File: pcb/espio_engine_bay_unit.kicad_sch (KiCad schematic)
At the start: 43 parts, among them U1 MCP2562-E-SN, U5 LF50CPT-TR

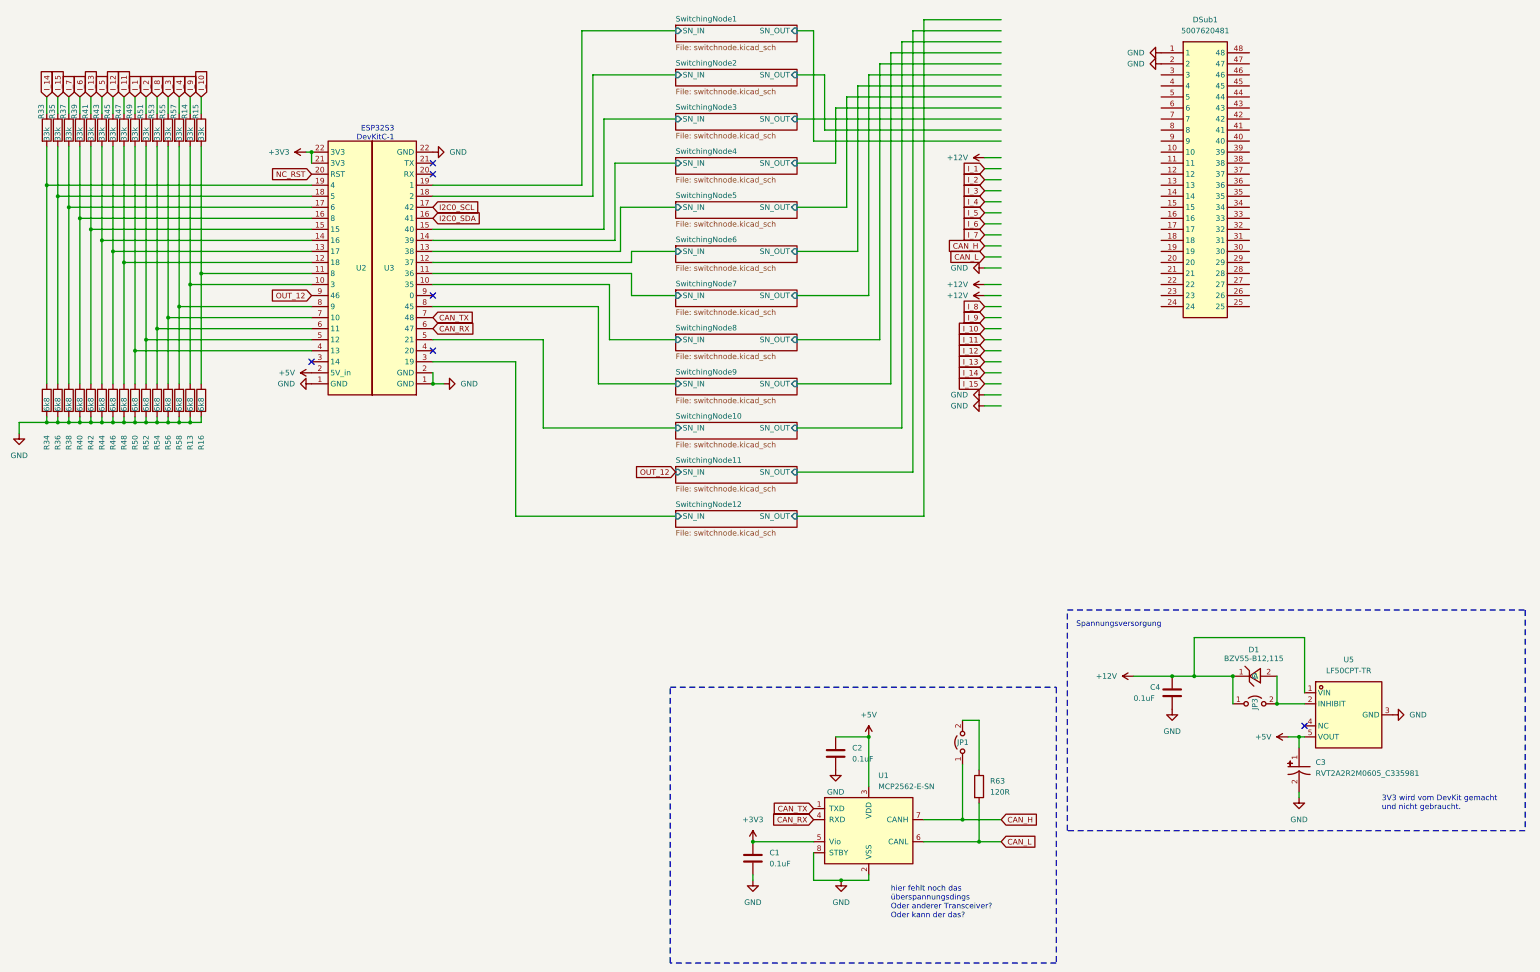
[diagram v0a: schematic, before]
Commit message: Add counters to ebu, update schematic
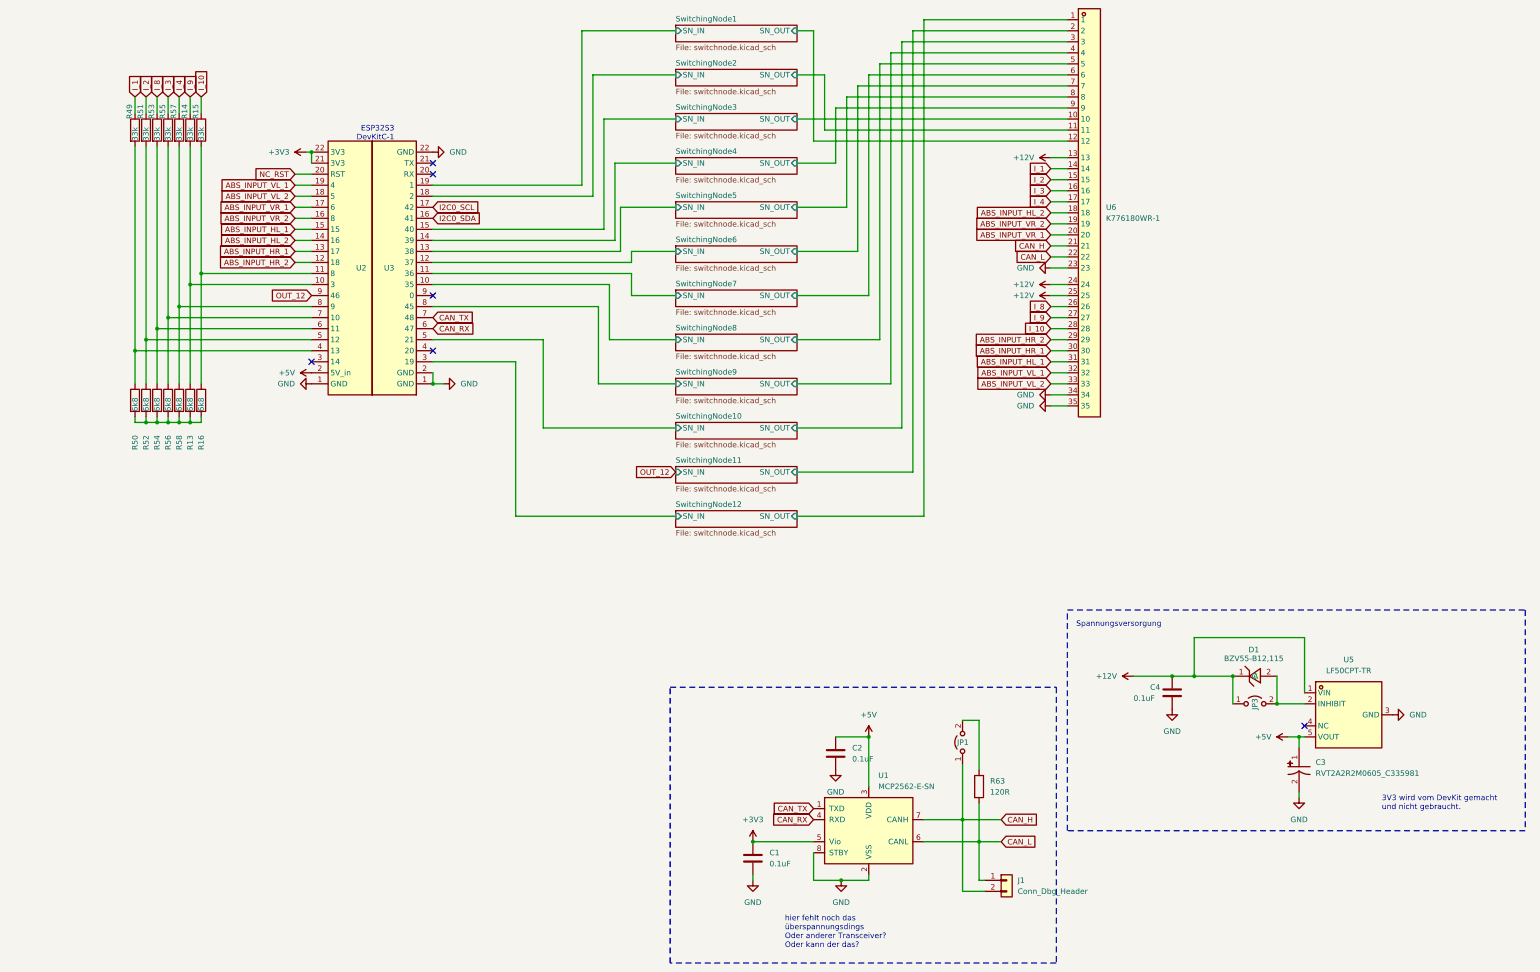
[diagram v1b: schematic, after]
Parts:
- removed DSub1: 5007620481, lcsc:CONN-TH_5007620481, symbol lcsc:5007620481
- removed R33, R35, R37, R39, R41, R43, R45, R47: 33k, Resistor_SMD:R_0603_1608Metric, symbol Device:R
- removed R34, R36, R38, R40, R42, R44, R46, R48: 6k8, Resistor_SMD:R_0603_1608Metric, symbol Device:R
- added J1: Conn_Dbg_Header, Connector_PinHeader_2.54mm:PinHeader_1x02_P2.54mm_Vertical_SMD_Pin1Left, symbol Connector_Generic:Conn_01x02
- added U6: K776180WR-1, lcsc:CONN-TH_35P-P4.00_K776180WR-2, symbol lcsc:K776180WR-1
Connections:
- net +12V: now also U6.13, U6.24, U6.25
- net CAN_H: now also J1.2 (Pin_2), U6.21
- net CAN_L: now also J1.1 (Pin_1), U6.22
- net GND: now also U6.23, U6.34, U6.35; no longer R13.2, R16.2, R50.2, R52.2, R54.2, R56.2, R58.2
- net I_1: now also U6.14
- net I_10: now also U6.28
- net I_2: now also U6.15
- net I_3: now also U6.16
- net I_4: now also U6.17
- net I_8: now also U6.26
- net I_9: now also U6.27
- net SwitchingNode1/SN_OUT: now also U6.12
- net SwitchingNode10/SN_OUT: now also U6.3
- net SwitchingNode11/SN_OUT: now also U6.2
- net SwitchingNode12/SN_OUT: now also U6.1
- net SwitchingNode2/SN_OUT: now also U6.11
- net SwitchingNode3/SN_OUT: now also U6.10
- net SwitchingNode4/SN_OUT: now also U6.9
- net SwitchingNode5/SN_OUT: now also U6.8
- net SwitchingNode6/SN_OUT: now also U6.7
- net SwitchingNode7/SN_OUT: now also U6.6
- net SwitchingNode8/SN_OUT: now also U6.5
- net SwitchingNode9/SN_OUT: now also U6.4
- net ABS_INPUT_HR_2: now reaches U2.12 (18)
- net ABS_INPUT_HR_2: now also U6.29
- net ABS_INPUT_HR_1: now reaches U2.13 (17)
- net ABS_INPUT_HR_1: now also U6.30
- net ABS_INPUT_HL_2: now reaches U2.14 (16)
- net ABS_INPUT_HL_2: now also U6.18
- net ABS_INPUT_HL_1: now reaches U2.15
- net ABS_INPUT_HL_1: now also U6.31
- net ABS_INPUT_VR_2: now reaches U2.16 (8)
- net ABS_INPUT_VR_2: now also U6.19
- net ABS_INPUT_VR_1: now reaches U2.17 (6)
- net ABS_INPUT_VR_1: now also U6.20
- net ABS_INPUT_VL_2: now reaches U2.18 (5)
- net ABS_INPUT_VL_2: now also U6.33
- net ABS_INPUT_VL_1: now reaches U2.19 (4)
- net ABS_INPUT_VL_1: now also U6.32
- new net: R13.2, R16.2, R50.2, R52.2, R54.2, R56.2, R58.2
